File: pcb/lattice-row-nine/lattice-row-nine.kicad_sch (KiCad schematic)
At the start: 22 parts, among them J1 Conn_ARM_SWD_TagConnect_TC203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, J2 USB_C_Receptacle_USB2.0_16P, U1 STM32G431KBUx, U2 AMS1117-3.3, U3 SRV05-4, Y1 16MHz

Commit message: Final production
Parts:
- U1: LCSC (none) -> C1341901

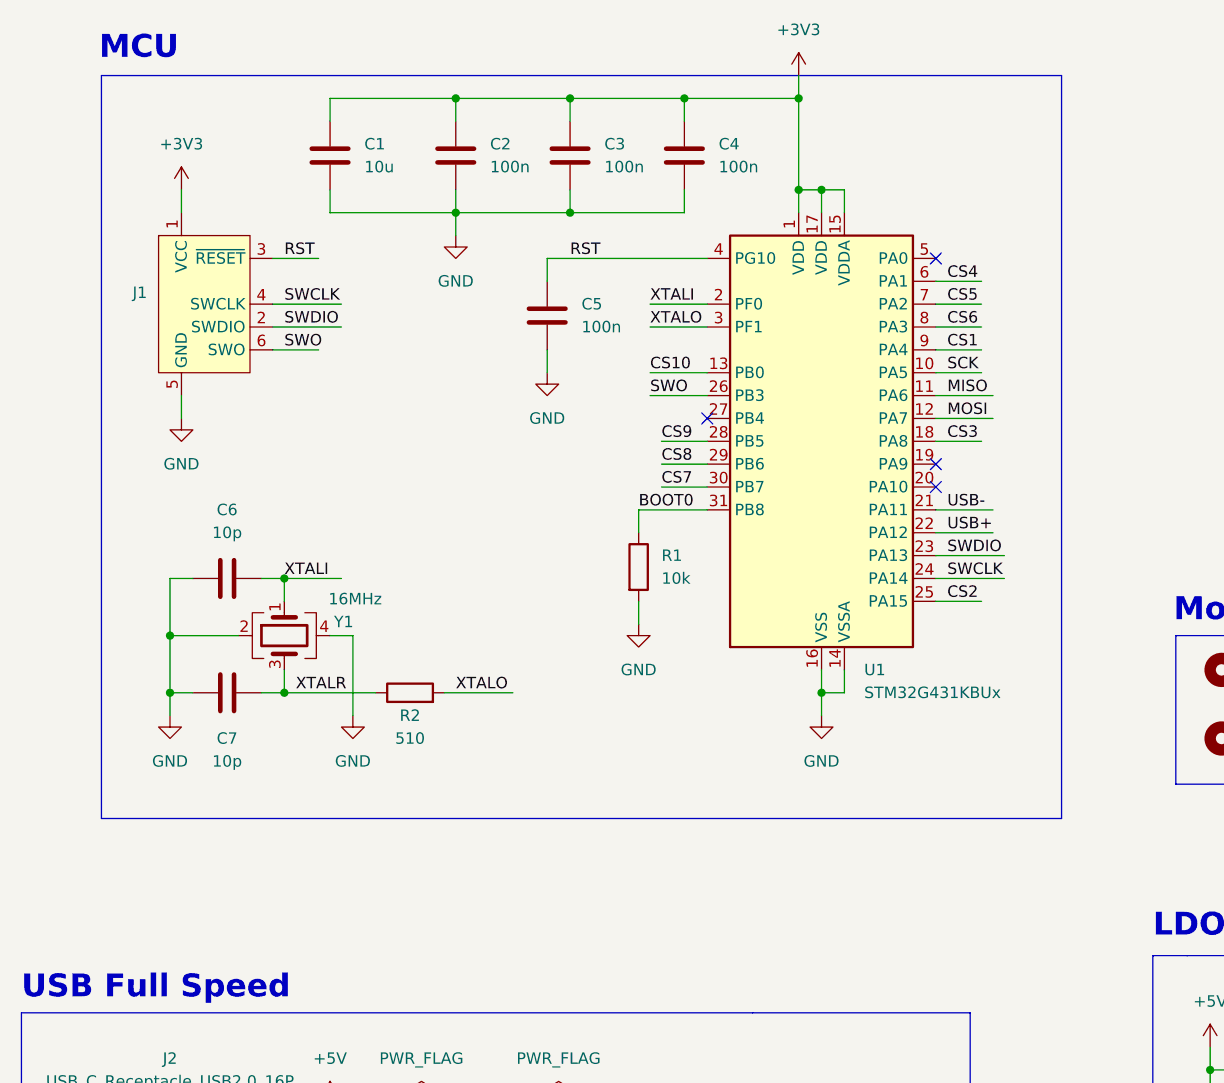
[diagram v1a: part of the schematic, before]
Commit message: Add part numbers
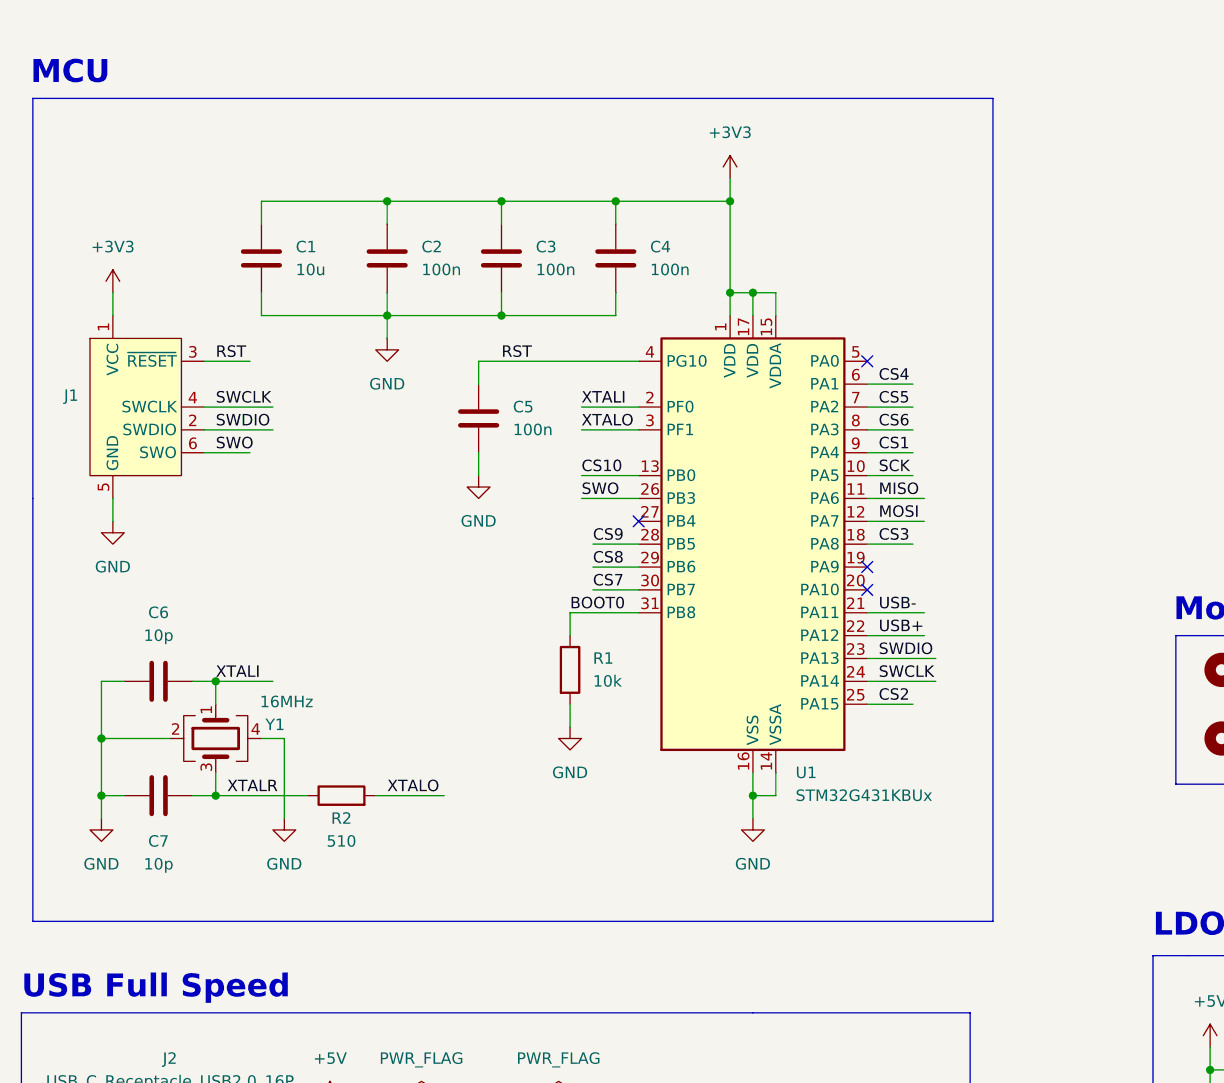
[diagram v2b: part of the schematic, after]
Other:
- moved on the sheet: C1, C2, C3, C4, C5, C6, C7, J1, R1, R2, U1, Y1
